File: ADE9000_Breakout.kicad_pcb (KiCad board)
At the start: 2 copper layers, 65 x 55 mm, 61 parts, among them J1 DIGITAL, J2 Voltage, J3 Voltage, J4 Voltage, U1 ADE9000, Y1 24.576MHz

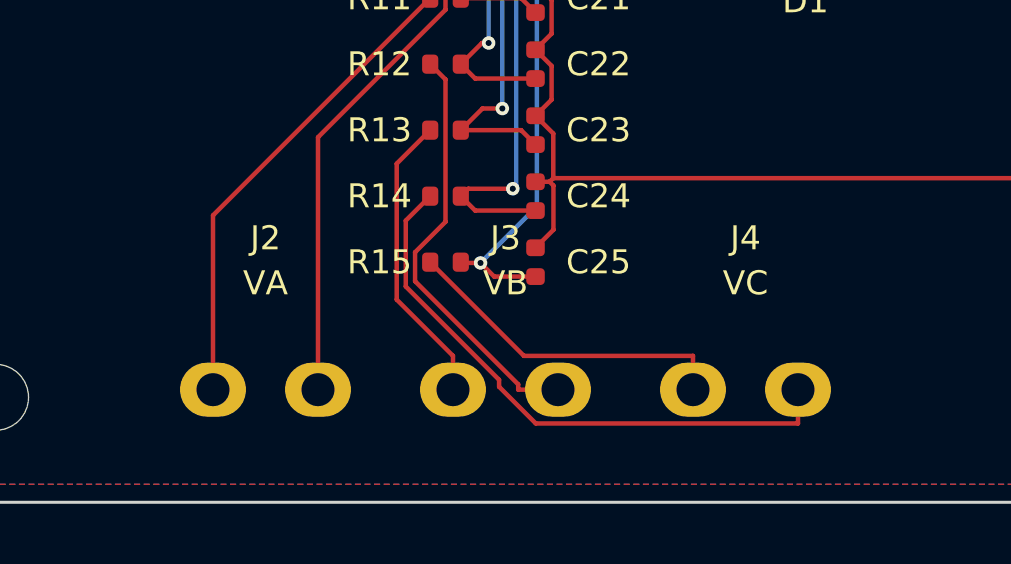
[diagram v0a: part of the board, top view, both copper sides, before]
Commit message: Add project-local 3D CAD assets
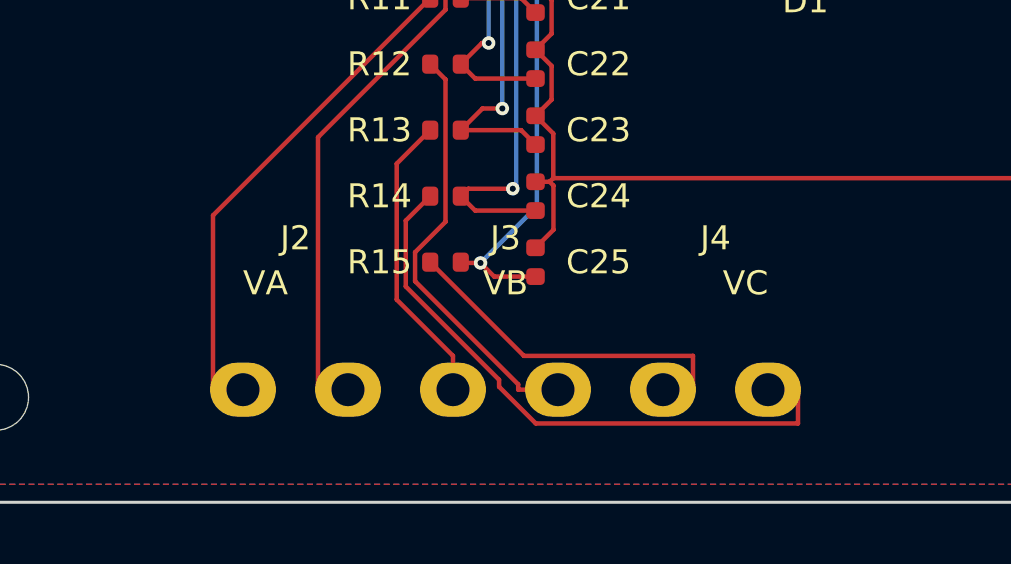
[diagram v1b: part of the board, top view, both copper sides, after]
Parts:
- moved J2 1.00 mm to (155.0, 131.2)
- moved J4 1.00 mm to (169.0, 131.2)
